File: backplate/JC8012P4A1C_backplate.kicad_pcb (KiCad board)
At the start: 2 copper layers, 242.8 x 158.7 mm, 12 parts

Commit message: Frame (CC BY-SA, based on thing:7208630): D-Sub cutout, bosses for the back plate, keyhole tabs removed; back plate holes matched to the frame
Co-Authored-By: Claude Opus 5.5 <noreply@anthropic.com>
Claude-Session: https://claude.ai/code/session_014h8cGi8SRWthYdGFH1Qgzz
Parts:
- moved H10 2.35 mm to (210.0, 23.6)
- moved H9 2.35 mm to (90.0, 23.6)
- moved H11 2.35 mm to (90.0, 176.3)
- moved H12 2.35 mm to (210.0, 176.3)
- moved H5 2.33 mm to (34.3, 26.4)
- moved H7 2.33 mm to (34.3, 173.6)
- moved H6 2.33 mm to (265.7, 26.4)
- moved H8 2.33 mm to (265.7, 173.6)

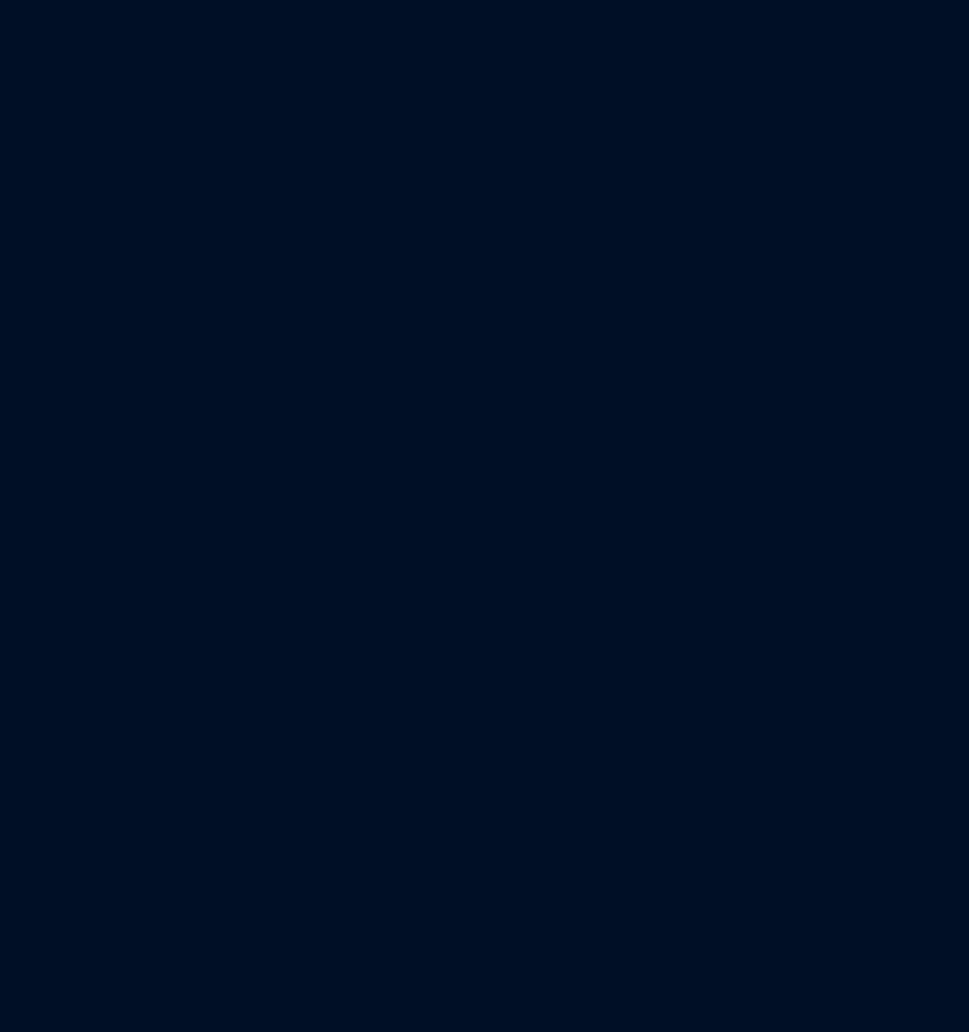
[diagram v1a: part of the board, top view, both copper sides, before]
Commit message: Back plate: speaker mount for XHXDZ-2828
- board-only footprint LS1: 4 x 2.7 mm on 23 x 23 mm (M2.5), 19 sound
  holes 2.0 mm, speaker on the inside next to the display cover on the
  CN3 side (frame +87/+30), checked in 3D against cover, frame and display
- renders and Gerber zip regenerated
- assembly BOM: speaker, 4 x M2.5x8, 4 x nut M2.5

Co-Authored-By: Claude Opus 5.5 <noreply@anthropic.com>
Claude-Session: https://claude.ai/code/session_014h8cGi8SRWthYdGFH1Qgzz
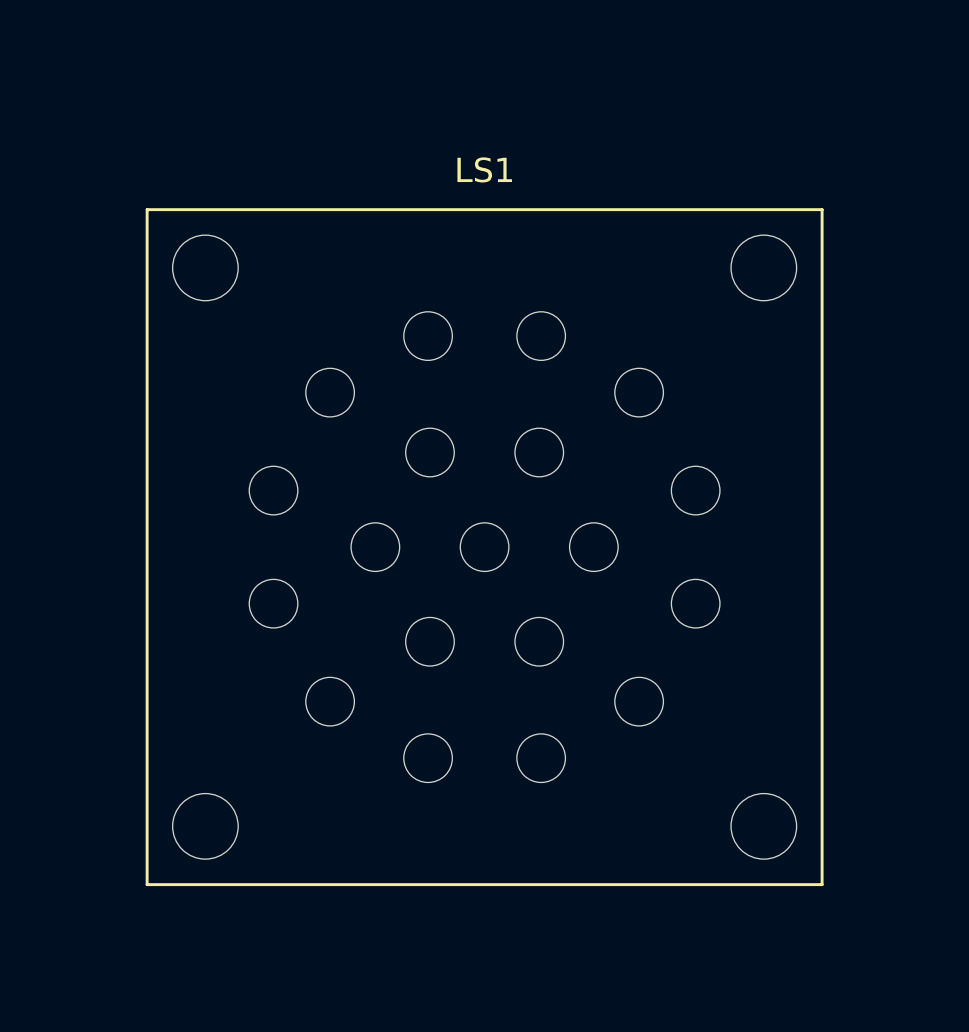
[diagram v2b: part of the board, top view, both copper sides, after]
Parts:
- added LS1: Speaker XHXDZ-2828, Backplate:Speaker_XHXDZ-2828_Mount, F.Cu at (237.0, 70.0)
